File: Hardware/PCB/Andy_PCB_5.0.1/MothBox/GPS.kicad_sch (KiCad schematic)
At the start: 10 parts, among them U10 Days, U11 Modes, U12 CD74HC4067M96E4, U13 Hours1, U14 Hours2, U8 GPs 5 pin PM2.54-1*5, U9 CD74HC4067M96E4

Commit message: days updates - schematic cleanups
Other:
- moved on the sheet: U14

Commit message: daily schematic updates
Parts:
- removed C8: 0.1uF, Capacitor_SMD:C_0805_2012Metric, symbol MB_Library:C_Small
- removed U12: CD74HC4067M96E4, easyeda2kicad:SOIC-24_L15.4-W7.5-P1.27-LS10.3-BL, symbol MB_Library:CD74HC4067M96E4
- removed U9: CD74HC4067M96E4, easyeda2kicad:SOIC-24_L15.4-W7.5-P1.27-LS10.3-BL, symbol MB_Library:CD74HC4067M96E4_1
- added C9: 0.1uF, Capacitor_SMD:C_0805_2012Metric, symbol MB_Library:C_Small
- added U15, U16: PCA9535PW, Package_SO:TSSOP-24_4.4x7.8mm_P0.65mm, symbol _pauls_library:PCA9535PW
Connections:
- net +3.3V: now also C9.2, U15.24 (VDD), U16.21 (A0), U16.24 (VDD)
- net Armed/Disarmed: now also U15.11 (IO0_7)
- net Attractor_1: now also U15.16 (IO1_3)
- net Attractor_2: now also U15.17 (IO1_4)
- net Attractor_3: now also U15.18 (IO1_5)
- net C1: now also U15.19 (IO1_6)
- net C2: now also U15.20 (IO1_7)
- net Fri: now also U15.6 (IO0_2)
- net GND: now also C9.1, U15.12 (VSS), U15.2 (A1), U15.21 (A0), U15.3 (A2), U16.12 (VSS), U16.2 (A1), U16.3 (A2)
- net HI/LOW_PWR: now also U15.14 (IO1_1)
- net Hour_1: now also U16.4 (IO0_0)
- net Hour_10: now also U16.14 (IO1_1)
- net Hour_11: now also U16.13 (IO1_0)
- net Hour_12: now also U16.16 (IO1_3)
- net Hour_13: now also U16.17 (IO1_4)
- net Hour_14: now also U16.18 (IO1_5)
- net Hour_15: now also U16.19 (IO1_6)
- net Hour_16: now also U16.20 (IO1_7)
- net Hour_2: now also U16.5 (IO0_1)
- net Hour_3: now also U16.6 (IO0_2)
- net Hour_4: now also U16.7 (IO0_3)
- net Hour_5: now also U16.8 (IO0_4)
- net Hour_6: now also U16.9 (IO0_5)
- net Hour_7: now also U16.10 (IO0_6)
- net Hour_8: now also U16.11 (IO0_7)
- net Hour_9: now also U16.15 (IO1_2)
- net INT/EXT_Attractor: now also U15.15 (IO1_2)
- net Mon: now also U15.10 (IO0_6)
- net Sat: now also U15.5 (IO0_1)
- net Sun: now also U15.4 (IO0_0)
- net Test_Debug: now also U15.13 (IO1_0)
- net Thur: now also U15.7 (IO0_3)
- net Tue: now also U15.9 (IO0_5)
- net Wed: now also U15.8 (IO0_4)
- new net SCL: U15.22 (SCL), U16.22 (SCL)
- new net SDA: U15.23 (SDA), U16.23 (SDA)
- no-connect marks 0 -> 2
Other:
- note added: "Can only use one GPS module at a time"
- note added: "GOOUUU Tech GPS Module"
- note added: "GPIO MUX"
- note added: "GY-NEO6MV2 GPS Module"
- note added: "HOURS"
- note added: "i2C Add: 0x20"
- note added: "i2C Add: 0x21"
- note added: "no GPIO interrupts needed."
- note removed: "Hours"
- note removed: "MUX"
- moved on the sheet: C7, H1, U10, U11, U13, U8

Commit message: updated photo LEDs and the power page
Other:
- company: (none) -> Digital Naturalism Laboritories
- title: (none) -> MothBox
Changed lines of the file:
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@@
 	(generator_version "9.0")
 	(paper "User" 330.2 228.6)
+	(title_block
+		(title "MothBox")
+		(date "2025-07-12")
+		(rev "5.0.1")
+		(company "Digital Naturalism Laboritories")
+	)
 	(rectangle
 		(start 27.432 120.65)

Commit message: updated footprints and schematic
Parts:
- C7, C9: symbol MB_Library:C_Small -> MothBox_Symbol_Library:C_Small; Digikey Part No 311-1140-2-ND -> (none); Digikey_Part_No (none) -> 311-1140-2-ND; LCSC Part no  C49678 -> (none); LCSC_Part_No (none) -> C49678
- H1: symbol MB_Library:2.54-1*4P母 -> MothBox_Symbol_Library:2.54-1*4P母; LCSC Part C2718488 -> (none); LCSC_Part (none) -> C2718488
- U10, U11, U13, U14: footprint easyeda2kicad:SW-SMD_SMXS-08K-TP -> easyeda_footprints:SW-SMD_SMXS-08K-TP; symbol MB_Library:SMXS-08K-TP -> MothBox_Symbol_Library:SMXS-08K-TP; LCSC Part C5439767 -> (none); LCSC_Part (none) -> C5439767
- U15, U16: symbol _pauls_library:PCA9535PW -> MothBox_Symbol_Library:PCA9535PW
- U8: symbol MB_Library:PM2.54-1*5 -> MothBox_Symbol_Library:PM2.54-1*5; LCSC Part C5116488 -> (none); LCSC_Part (none) -> C5116488

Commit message: daily PCB update
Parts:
- C7, C9: footprint Capacitor_SMD:C_0805_2012Metric -> MothBox_footprints_Library:C_0603_1608Metric; LCSC_Part_No C49678 -> C3011704
- H1: value GPS 4 pin 2.54-1*4P母 -> GPS 4 pin 2.54-1*4P; footprint AQLibrary:GPS4pin_HDR-TH_4P-P2.54-V-F -> Connector_PinSocket_2.54mm:PinSocket_1x04_P2.54mm_Vertical
- U10, U11, U13, U14: footprint easyeda_footprints:SW-SMD_SMXS-08K-TP -> MothBox_footprints_Library:SW-SMD_SMXS-08K-TP
- U15, U16: footprint Package_SO:TSSOP-24_4.4x7.8mm_P0.65mm -> MothBox_footprints_Library:TSSOP-24_4.4x7.8mm_P0.65mm
- U8: footprint AQLibrary:GPS5pin_HDR-TH_5P-P2.54-V-F -> Connector_PinSocket_2.54mm:PinSocket_1x05_P2.54mm_Vertical
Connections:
- net Armed/Disarmed: now also U15.4 (IO0_0); no longer U15.11 (IO0_7)
- net Attractor_1: now also U15.17 (IO1_4); no longer U15.16 (IO1_3)
- net Attractor_2: now also U15.16 (IO1_3); no longer U15.17 (IO1_4)
- net Attractor_3: now also U15.15 (IO1_2); no longer U15.18 (IO1_5)
- net C1: now also U15.14 (IO1_1); no longer U15.19 (IO1_6)
- net C2: now also U15.13 (IO1_0); no longer U15.20 (IO1_7)
- net Fri: now also U15.9 (IO0_5); no longer U15.6 (IO0_2)
- net HI/LOW_PWR: now also U15.19 (IO1_6); no longer U15.14 (IO1_1)
- net INT/EXT_Attractor: now also U15.18 (IO1_5); no longer U15.15 (IO1_2)
- net Mon: now also U15.5 (IO0_1); no longer U15.10 (IO0_6)
- net Sat: now also U15.10 (IO0_6); no longer U15.5 (IO0_1)
- net Sun: now also U15.11 (IO0_7); no longer U15.4 (IO0_0)
- net Test_Debug: now also U15.20 (IO1_7); no longer U15.13 (IO1_0)
- net Thur: now also U15.8 (IO0_4); no longer U15.7 (IO0_3)
- net Tue: now also U15.6 (IO0_2); no longer U15.9 (IO0_5)
- net Wed: now also U15.7 (IO0_3); no longer U15.8 (IO0_4)
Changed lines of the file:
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@@
 	)
 	(label "Attractor_3"
-		(at 78.74 176.53 0)
+		(at 78.74 168.91 0)
 		(effects
 			(font
@@
 	)
 	(label "Fri"
-		(at 78.74 146.05 0)
+		(at 78.74 153.67 0)
 		(effects
 			(font
@@
 	)
 	(label "Wed"
-		(at 78.74 151.13 0)
+		(at 78.74 148.59 0)
 		(effects
 			(font
@@
 	)
 	(label "Test_Debug"
-		(at 78.74 163.83 0)
+		(at 78.74 181.61 0)
 		(effects
 			(font
@@
 	)
 	(label "Thur"
-		(at 78.74 148.59 0)
+		(at 78.74 151.13 0)
 		(effects
 			(font
@@
 	)
 	(label "Armed{slash}Disarmed"
-		(at 78.74 158.75 0)
+		(at 78.74 140.97 0)
 		(effects
 			(font
@@
 	)
 	(label "Tue"
-		(at 78.74 153.67 0)
+		(at 78.74 146.05 0)
 		(effects
 			(font
@@
 	)
 	(label "Sat"
-		(at 78.74 143.51 0)
+		(at 78.74 156.21 0)
 		(effects
 			(font
@@
 	)
 	(label "HI{slash}LOW_PWR"
-		(at 78.74 166.37 0)
+		(at 78.74 179.07 0)
 		(effects
 			(font
@@
 	)
 	(label "Mon"
-		(at 78.74 156.21 0)
+		(at 78.74 143.51 0)
 		(effects
 			(font
@@
 	)
 	(label "C2"
-		(at 78.74 181.61 0)
+		(at 78.74 163.83 0)
 		(effects
 			(font
@@
 	)
 	(label "C1"
-		(at 78.74 179.07 0)
+		(at 78.74 166.37 0)
 		(effects
 			(font
@@
 	)
 	(label "Attractor_2"
-		(at 78.74 173.99 0)
+		(at 78.74 171.45 0)
 		(effects
 			(font
@@
 	)
 	(label "Sun"
-		(at 78.74 140.97 0)
+		(at 78.74 158.75 0)
 		(effects
 			(font
@@
 	)
 	(label "Attractor_1"
-		(at 78.74 171.45 0)
+		(at 78.74 173.99 0)
 		(effects
 			(font
@@
 	)
 	(label "INT{slash}EXT_Attractor"
-		(at 78.74 168.91 0)
+		(at 78.74 176.53 0)
 		(effects
 			(font
@@
 			)
 		)
-		(property "Value" "GPS 4 pin 2.54-1*4P母"
+		(property "Value" "GPS 4 pin 2.54-1*4P"
 			(at 53.34 57.1499 0)
 			(effects
@@
 			)
 		)
-		(property "Footprint" "AQLibrary:GPS4pin_HDR-TH_4P-P2.54-V-F"
+		(property "Footprint" "Connector_PinSocket_2.54mm:PinSocket_1x04_P2.54mm_Vertical"
 			(at 49.53 67.31 0)
 			(effects
@@
 			)
 		)
+		(property "Ali_Express_Link" ""
+			(at 49.53 55.88 0)
+			(effects
+				(font
+					(size 1.27 1.27)
+				)
+				(hide yes)
+			)
+		)
+		(property "LCSC_PN" ""
+			(at 49.53 55.88 0)
+			(effects
+				(font
+					(size 1.27 1.27)
+				)
+				(hide yes)
+			)
+		)
 		(pin "4"
 		)
@@
 			)
 		)
-		(property "Footprint" "Capacitor_SMD:C_0805_2012Metric"
+		(property "Footprint" "MothBox_footprints_Library:C_0603_1608Metric"
 			(at 48.26 138.43 0)
 			(effects
@@
 			)
 		)
-		(property "LCSC_Part_No" "C49678"
+		(property "LCSC_Part_No" "C3011704"
+			(at 48.26 138.43 0)
+			(effects
+				(font
+					(size 1.27 1.27)
+				)
+				(hide yes)
+			)
+		)
+		(property "Ali_Express_Link" ""
+			(at 48.26 138.43 0)
+			(effects
+				(font
+					(size 1.27 1.27)
+				)
+				(hide yes)
+			)
+		)
+		(property "LCSC_PN" ""
 			(at 48.26 138.43 0)
 			(effects
@@
 			)
 		)
-		(property "Footprint" "easyeda_footprints:SW-SMD_SMXS-08K-TP"
+		(property "Footprint" "MothBox_footprints_Library:SW-SMD_SMXS-08K-TP"
 			(at 289.56 97.79 0)
 			(effects
@@
 			)
 		)
+		(property "Ali_Express_Link" ""
+			(at 289.56 80.01 0)
+			(effects
+				(font
+					(size 1.27 1.27)
+				)
+				(hide yes)
+			)
+		)
+		(property "LCSC_PN" ""
+			(at 289.56 80.01 0)
+			(effects
+				(font
+					(size 1.27 1.27)
+				)
+				(hide yes)
+			)
+		)
 		(pin "7"
 		)
@@
 			)
 		)
-		(property "Footprint" "AQLibrary:GPS5pin_HDR-TH_5P-P2.54-V-F"
+		(property "Footprint" "Connector_PinSocket_2.54mm:PinSocket_1x05_P2.54mm_Vertical"
 			(at 49.53 96.52 0)
 			(effects
@@
 			)
 		)
+		(property "Ali_Express_Link" ""
+			(at 49.53 83.82 0)
+			(effects
+				(font
+					(size 1.27 1.27)
+				)
+				(hide yes)
+			)
+		)
+		(property "LCSC_PN" ""
+			(at 49.53 83.82 0)
+			(effects
+				(font
+					(size 1.27 1.27)
+				)
+				(hide yes)
+			)
+		)
 		(pin "2"
 		)
@@
 			)
 		)
-		(property "Footprint" "Package_SO:TSSOP-24_4.4x7.8mm_P0.65mm"
+		(property "Footprint" "MothBox_footprints_Library:TSSOP-24_4.4x7.8mm_P0.65mm"
 			(at 144.78 140.97 0)
 			(effects
@@
 			)
 		)
+		(property "Ali_Express_Link" ""
+			(at 146.05 140.97 0)
+			(effects
+				(font
+					(size 1.27 1.27)
+				)
+				(hide yes)
+			)
+		)
+		(property "LCSC_PN" ""
+			(at 146.05 140.97 0)
+			(effects
+				(font
+					(size 1.27 1.27)
+				)
+				(hide yes)
+			)
+		)
 		(pin "5"
 		)
@@
 			)
 		)
-		(property "Footprint" "easyeda_footprints:SW-SMD_SMXS-08K-TP"
+		(property "Footprint" "MothBox_footprints_Library:SW-SMD_SMXS-08K-TP"
 			(at 181.61 97.79 0)
 			(effects
@@
 			)
 		)
+		(property "Ali_Express_Link" ""
+			(at 181.61 80.01 0)
+			(effects
+				(font
+					(size 1.27 1.27)
+				)
+				(hide yes)
+			)
+		)
+		(property "LCSC_PN" ""
+			(at 181.61 80.01 0)
+			(effects
+				(font
+					(size 1.27 1.27)
+				)
+				(hide yes)
+			)
+		)
 		(pin "7"
 		)
@@
 			)
 		)
-		(property "Footprint" "easyeda_footprints:SW-SMD_SMXS-08K-TP"
+		(property "Footprint" "MothBox_footprints_Library:SW-SMD_SMXS-08K-TP"
 			(at 237.49 97.79 0)
 			(effects
@@
 			)
 		)
+		(property "Ali_Express_Link" ""
+			(at 237.49 80.01 0)
+			(effects
+				(font
+					(size 1.27 1.27)
+				)
+				(hide yes)
+			)
+		)
+		(property "LCSC_PN" ""
+			(at 237.49 80.01 0)
+			(effects
+				(font
+					(size 1.27 1.27)
+				)
+				(hide yes)
+			)
+		)
 		(pin "7"
 		)
@@
 			)
 		)
-		(property "Footprint" "easyeda_footprints:SW-SMD_SMXS-08K-TP"
+		(property "Footprint" "MothBox_footprints_Library:SW-SMD_SMXS-08K-TP"
 			(at 130.81 97.79 0)
 			(effects
@@
 			)
 		)
+		(property "Ali_Express_Link" ""
+			(at 130.81 80.01 0)
+			(effects
+				(font
+					(size 1.27 1.27)
+				)
+				(hide yes)
+			)
+		)
+		(property "LCSC_PN" ""
+			(at 130.81 80.01 0)
+			(effects
+				(font
+					(size 1.27 1.27)
+				)
+				(hide yes)
+			)
+		)
 		(pin "7"
 		)
@@
 			)
 		)
-		(property "Footprint" "Capacitor_SMD:C_0805_2012Metric"
+		(property "Footprint" "MothBox_footprints_Library:C_0603_1608Metric"
 			(at 129.54 138.43 0)
 			(effects
@@
 			)
 		)
-		(property "LCSC_Part_No" "C49678"
+		(property "LCSC_Part_No" "C3011704"
+			(at 129.54 138.43 0)
+			(effects
+				(font
+					(size 1.27 1.27)
+				)
+				(hide yes)
+			)
+		)
+		(property "Ali_Express_Link" ""
+			(at 129.54 138.43 0)
+			(effects
+				(font
+					(size 1.27 1.27)
+				)
+				(hide yes)
+			)
+		)
+		(property "LCSC_PN" ""
 			(at 129.54 138.43 0)
 			(effects
@@
 			)
 		)
-		(property "Footprint" "Package_SO:TSSOP-24_4.4x7.8mm_P0.65mm"
+		(property "Footprint" "MothBox_footprints_Library:TSSOP-24_4.4x7.8mm_P0.65mm"
 			(at 63.5 140.97 0)
 			(effects
@@
 			(at 64.77 140.97 0)
 			(effects
+				(font
+					(size 1.27 1.27)
+				)
+				(hide yes)
+			)
+		)
+		(property "Ali_Express_Link" ""
+			(at 64.77 140.97 0)
+			(effects
+				(font
+					(size 1.27 1.27)
+				)
+				(hide yes)
+			)
+		)
+		(property "LCSC_PN" ""
+			(at 64.77 140.97 0)
+			(effects

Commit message: adding in datasheets
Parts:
- U16: LCSC (none) -> C42420616
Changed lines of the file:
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@@
+			)
+		)
+		(property "LCSC" "C42420616"
+			(at 146.05 140.97 0)
+			(effects
+				(font
+					(size 1.27 1.27)
+				)
+				(hide yes)
 			)
 		)

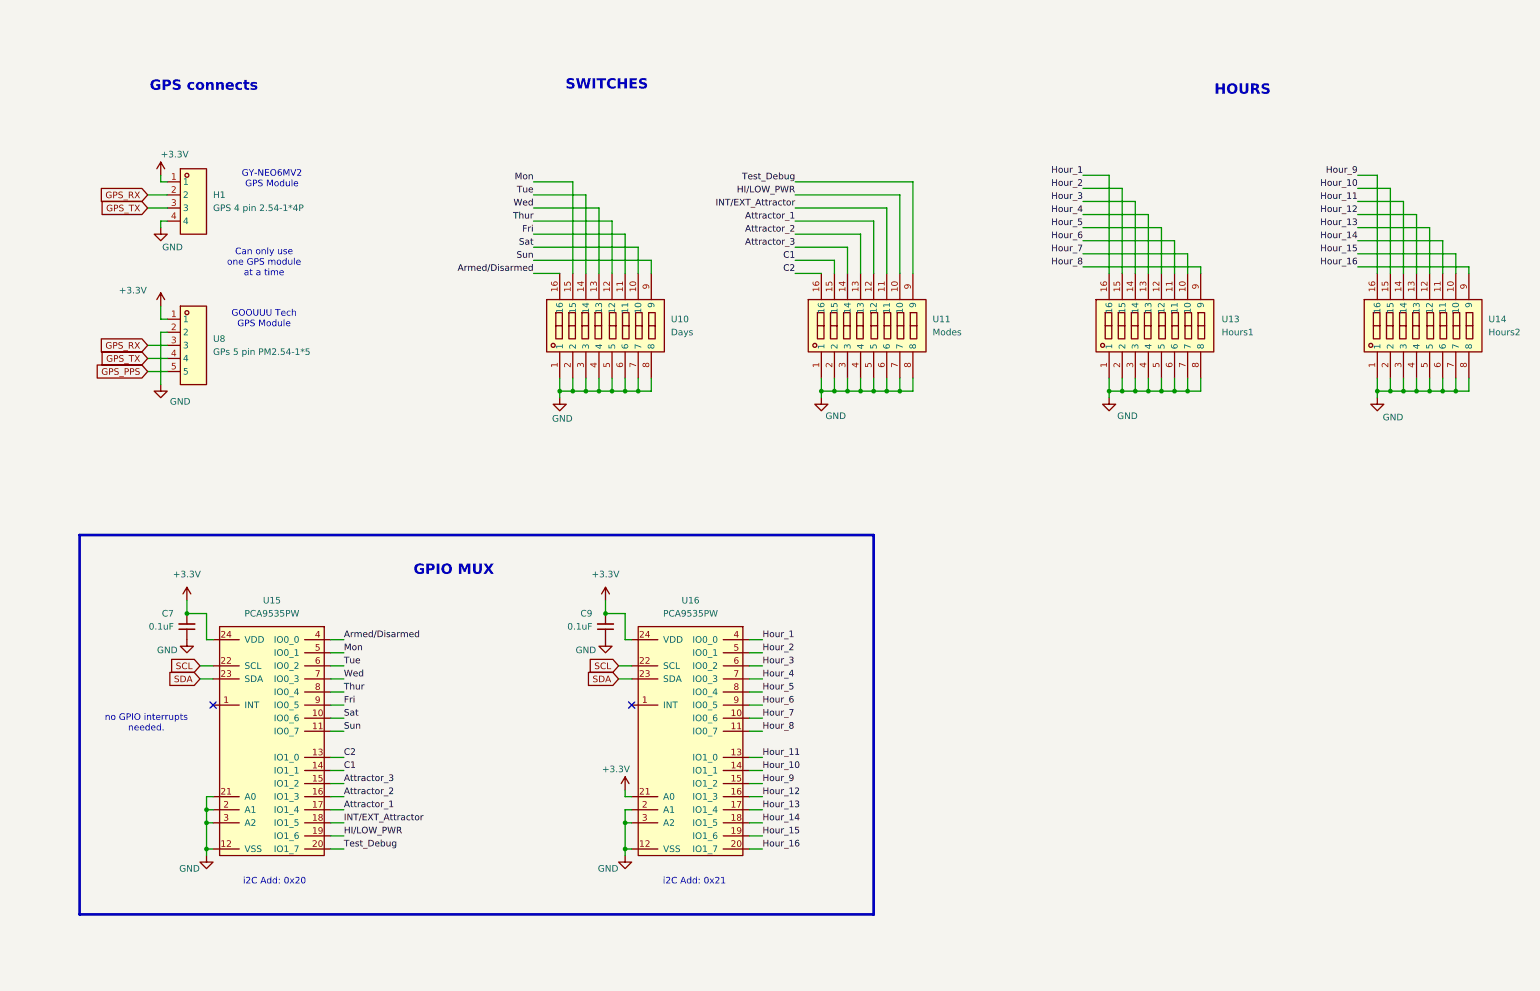
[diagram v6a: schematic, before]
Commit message: added in extra hour switch for 24hr coverage
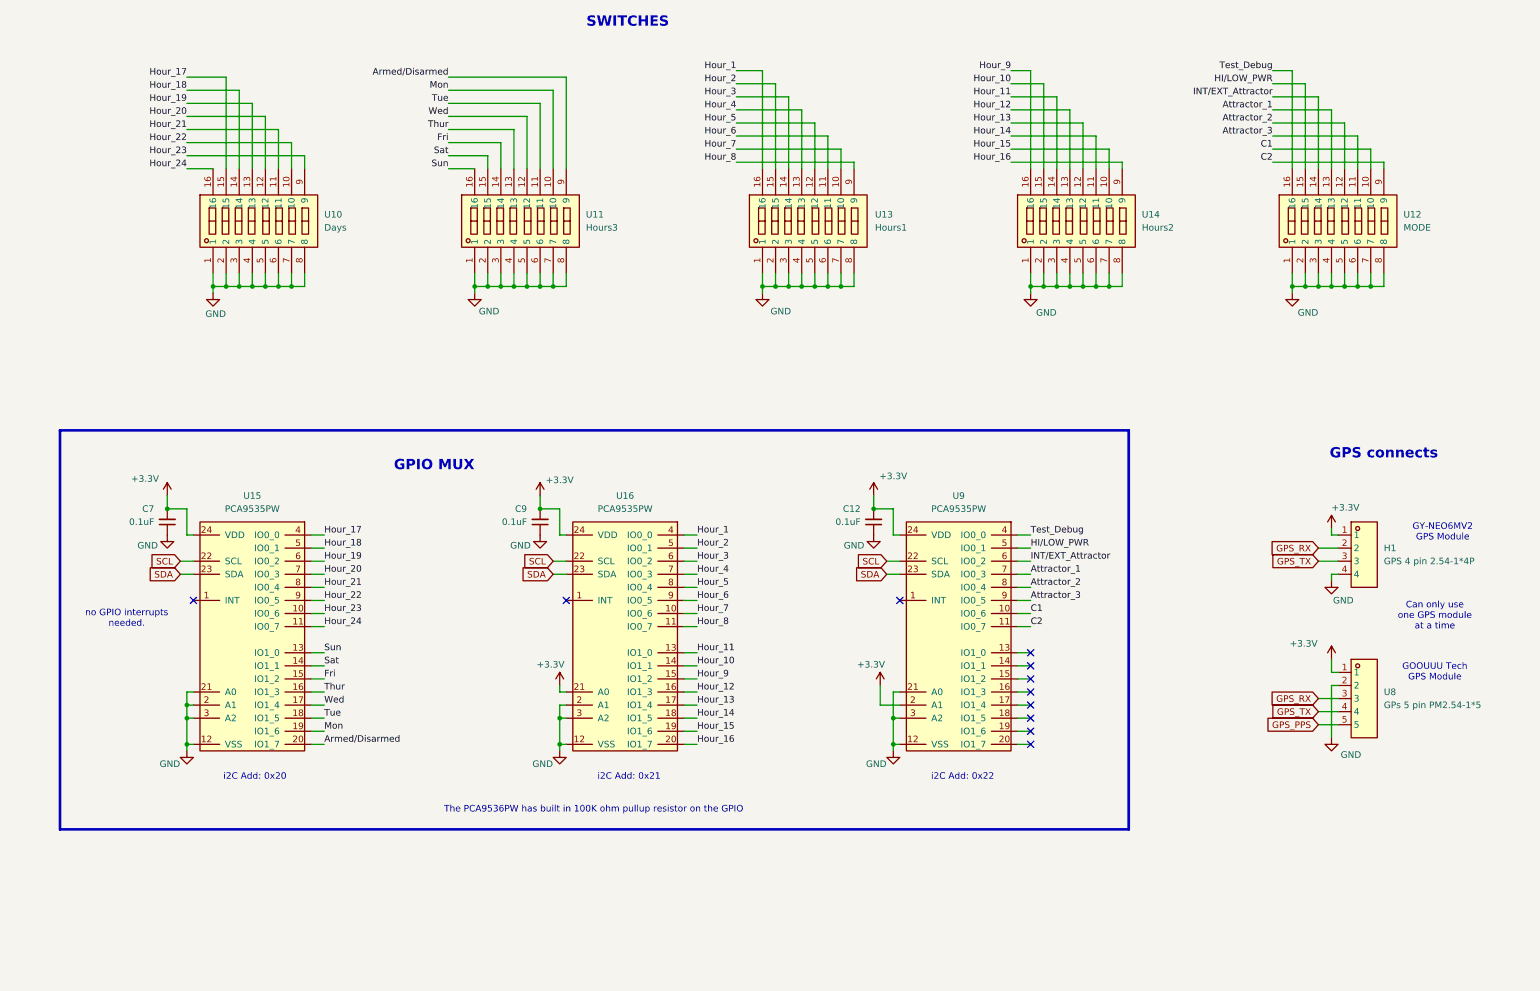
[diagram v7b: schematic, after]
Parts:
- added C12: 0.1uF, MothBox_footprints_Library:C_0603_1608Metric, symbol MothBox_Symbol_Library:C_Small
- added U12: MODE, MothBox_footprints_Library:SW-SMD_SMXS-08K-TP, symbol MothBox_Symbol_Library:SMXS-08K-TP
- added U9: PCA9535PW, MothBox_footprints_Library:TSSOP-24_4.4x7.8mm_P0.65mm, symbol MothBox_Symbol_Library:PCA9535PW
- C7, C9: LCSC_Part (none) -> C14663; LCSC_Part_No C3011704 -> (none)
- U11: value Modes -> Hours3
- U15: LCSC_Part (none) -> C255606
- U16: LCSC C42420616 -> (none); LCSC_Part (none) -> C255606
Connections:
- net +3.3V: now also C12.2, U9.2 (A1), U9.24 (VDD)
- net Armed/Disarmed: now also U11.9, U15.20 (IO1_7); no longer U10.16, U15.4 (IO0_0)
- net Attractor_1: now also U12.13, U9.7 (IO0_3); no longer U11.12, U15.17 (IO1_4)
- net Attractor_2: now also U12.12, U9.8 (IO0_4); no longer U11.13, U15.16 (IO1_3)
- net Attractor_3: now also U12.11, U9.9 (IO0_5); no longer U11.14, U15.15 (IO1_2)
- net C1: now also U12.10, U9.10 (IO0_6); no longer U11.15, U15.14 (IO1_1)
- net C2: now also U12.9, U9.11 (IO0_7); no longer U11.16, U15.13 (IO1_0)
- net Fri: now also U11.14, U15.15 (IO1_2); no longer U10.11, U15.9 (IO0_5)
- net GND: now also C12.1, U12.1, U12.2, U12.3, U12.4, U12.5, U12.6, U12.7, U12.8, U9.12 (VSS), U9.21 (A0), U9.3 (A2)
- net HI/LOW_PWR: now also U12.15, U9.5 (IO0_1); no longer U11.10, U15.19 (IO1_6)
- net INT/EXT_Attractor: now also U12.14, U9.6 (IO0_2); no longer U11.11, U15.18 (IO1_5)
- net Mon: now also U11.10, U15.19 (IO1_6); no longer U10.15, U15.5 (IO0_1)
- net SCL: now also U9.22 (SCL)
- net SDA: now also U9.23 (SDA)
- net Sat: now also U11.15, U15.14 (IO1_1); no longer U10.10, U15.10 (IO0_6)
- net Sun: now also U11.16, U15.13 (IO1_0); no longer U10.9, U15.11 (IO0_7)
- net Test_Debug: now also U12.16, U9.4 (IO0_0); no longer U11.9, U15.20 (IO1_7)
- net Thur: now also U11.13, U15.16 (IO1_3); no longer U10.12, U15.8 (IO0_4)
- net Tue: now also U11.11, U15.18 (IO1_5); no longer U10.14, U15.6 (IO0_2)
- net Wed: now also U11.12, U15.17 (IO1_4); no longer U10.13, U15.7 (IO0_3)
- new net Hour_17: U10.15, U15.4 (IO0_0)
- new net Hour_18: U10.14, U15.5 (IO0_1)
- new net Hour_19: U10.13, U15.6 (IO0_2)
- new net Hour_20: U10.12, U15.7 (IO0_3)
- new net Hour_21: U10.11, U15.8 (IO0_4)
- new net Hour_22: U10.10, U15.9 (IO0_5)
- new net Hour_23: U10.9, U15.10 (IO0_6)
- new net Hour_24: U10.16, U15.11 (IO0_7)
- no-connect marks 2 -> 11
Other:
- note added: "The PCA9536PW has built in 100K ohm pullup resistor on the GPIO"
- note added: "i2C Add: 0x22"
- note removed: "HOURS"
- moved on the sheet: C7, C9, H1, U10, U11, U13, U14, U15, U16, U8

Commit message: before trimming top of PCB
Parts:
- added C13: 0.1uF, MothBox_footprints_Library:C_0603_1608Metric, symbol MothBox_Symbol_Library:C_Small
- added U17: BH1750FVI-TR, easyeda2kicad:WSOF-6_L2.6-W1.6-P0.50-TL-EP, symbol easyeda2kicad:BH1750FVI-TR
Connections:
- net +3.3V: now also C13.2, U17.1 (VCC)
- net GND: now also C13.1, U17.2 (ADDR), U17.3 (GND)
- net SCL: now also U17.6 (SCL)
- net SDA: now also U17.4 (SDA)
- no-connect marks 11 -> 13
